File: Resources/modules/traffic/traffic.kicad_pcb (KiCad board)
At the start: 2 copper layers, 23.1 x 25.4 mm, 11 parts, among them J1 Conn_01x06_Male, J2 Conn_01x02_Male, J3 Conn_01x01_Male, Q1 MMBT3906

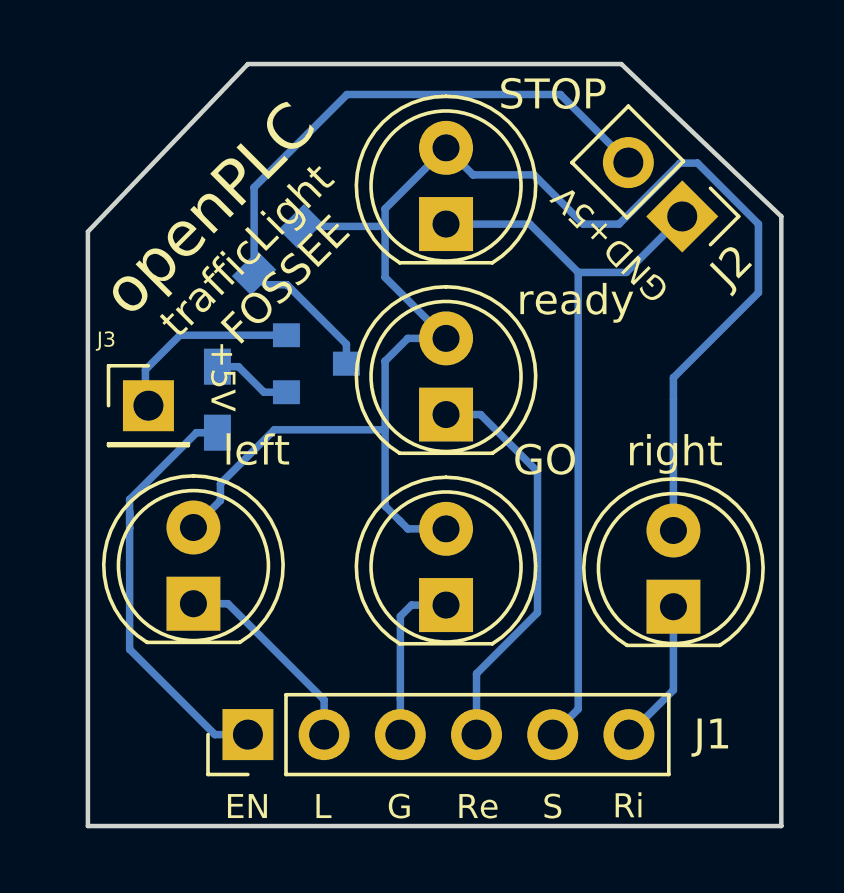
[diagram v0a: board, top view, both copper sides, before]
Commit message: label correction&additions in traffic&switches modules. Updated gerbers - both V1 and modules
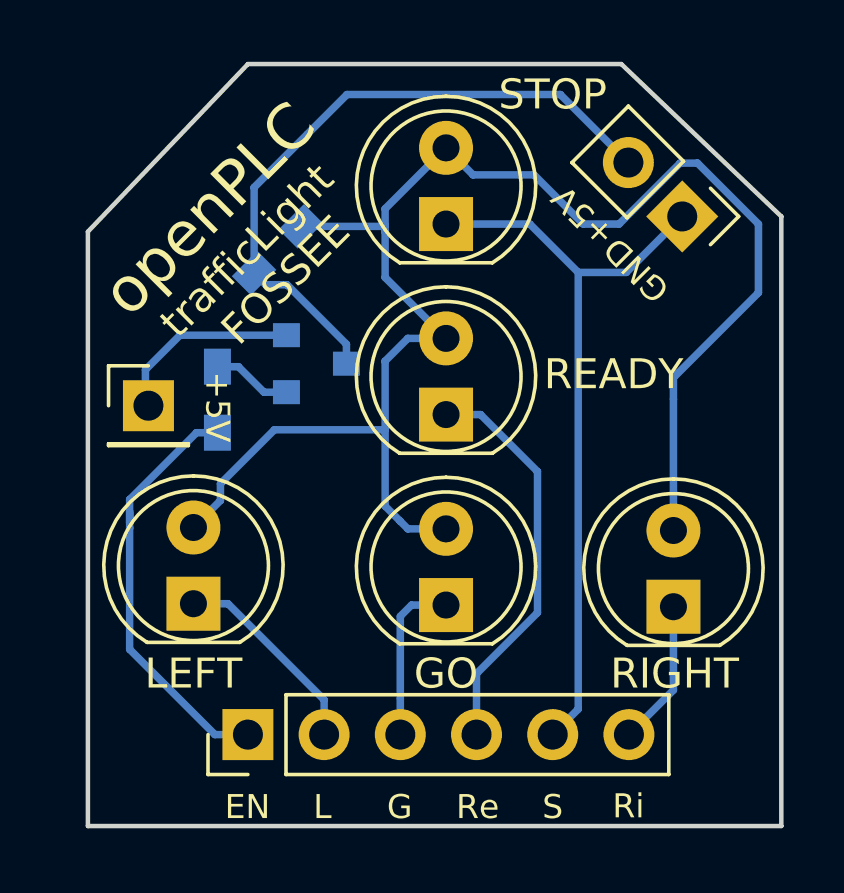
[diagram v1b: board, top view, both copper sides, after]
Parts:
- D1: value left -> LEFT
- D3: value right -> RIGHT
- D4: value ready -> READY
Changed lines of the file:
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@@
     (descr "Through hole straight socket strip, 1x01, 2.54mm pitch, single row")
     (tags "Through hole socket strip THT 1x01 2.54mm single row")
-    (fp_text reference J3 (at -1.4 -2.2) (layer F.SilkS)
+    (fp_text reference J3 (at -1.4 -2.2) (layer F.SilkS) hide
       (effects (font (size 0.5 0.5) (thickness 0.125)))
     )
@@
     (descr "Through hole straight socket strip, 1x02, 2.54mm pitch, single row")
     (tags "Through hole socket strip THT 1x02 2.54mm single row")
-    (fp_text reference J2 (at 0 -2.33 225) (layer F.SilkS)
+    (fp_text reference J2 (at 0 -2.33 225) (layer F.SilkS) hide
       (effects (font (size 1 1) (thickness 0.15)))
     )
@@
       (effects (font (size 1 1) (thickness 0.15)))
     )
-    (fp_text value ready (at 3.81 4.318 180) (layer F.SilkS)
+    (fp_text value READY (at 1.3425 5.588 180) (layer F.SilkS)
       (effects (font (size 1 1) (thickness 0.15)))
     )
@@
       (effects (font (size 1 1) (thickness 0.15)))
     )
-    (fp_text value right (at 5.175 0.04 180) (layer F.SilkS)
+    (fp_text value RIGHT (at -2.232 0.04 180) (layer F.SilkS)
       (effects (font (size 1 1) (thickness 0.15)))
     )
@@
       (effects (font (size 1 1) (thickness 0.15)))
     )
-    (fp_text value GO (at 4.826 3.302 180) (layer F.SilkS)
+    (fp_text value GO (at -2.286 0 180) (layer F.SilkS)
       (effects (font (size 1 1) (thickness 0.15)))
     )
@@
       (effects (font (size 1 1) (thickness 0.15)))
     )
-    (fp_text value left (at 5.1 2.1 180) (layer F.SilkS)
+    (fp_text value LEFT (at -2.332 0 180) (layer F.SilkS)
       (effects (font (size 1 1) (thickness 0.15)))
     )
@@
     (descr "Through hole straight socket strip, 1x06, 2.54mm pitch, single row")
     (tags "Through hole socket strip THT 1x06 2.54mm single row")
-    (fp_text reference J1 (at 0 15.494 180) (layer F.SilkS)
+    (fp_text reference J1 (at 0 15.494 180) (layer F.SilkS) hide
       (effects (font (size 1 1) (thickness 0.15)))
     )
@@
     )
   )
-  (gr_text +5V (at 139.870711 93.716339 270) (layer F.SilkS)
+  (gr_text +5V (at 139.7 94.742 270) (layer F.SilkS)
     (effects (font (size 0.8 0.8) (thickness 0.1)))
   )
